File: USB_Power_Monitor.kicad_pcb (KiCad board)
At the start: 4 copper layers, 46.1 x 21 mm, 55 parts, among them IC1 MCS1826GQTE-05-P, J1 USB_C_Receptacle, J2 USB_C_Plug, J5 Conn_01x01, J6 Conn_01x01, U1 RP2040, U2 L7983PU33R, U3 W25Q16JVSS, U4 TS3USB221AQRSERQ1, Y1 ABM8-272-T3

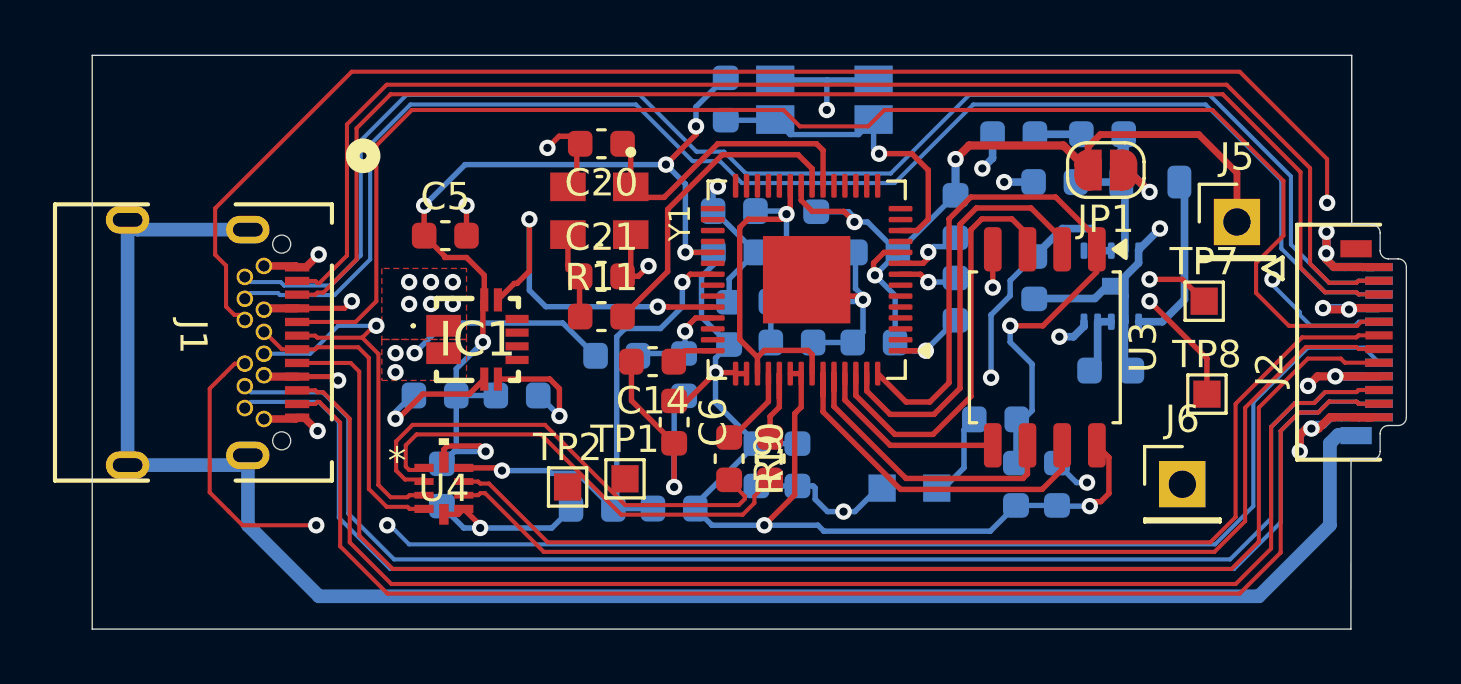
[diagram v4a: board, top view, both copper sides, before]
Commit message: Fixed overlapping silkscreen
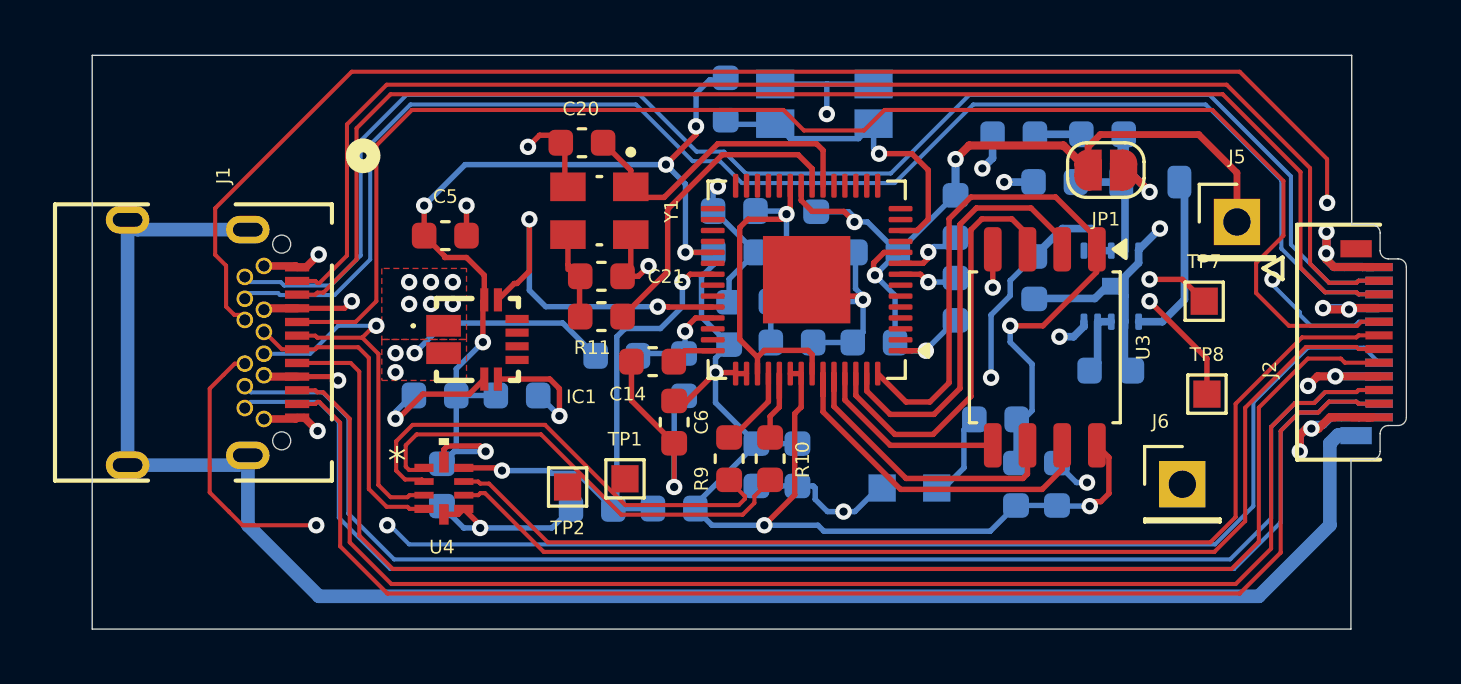
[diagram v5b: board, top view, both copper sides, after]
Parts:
- moved C20 0.71 mm to (144.9, 90.7)
- moved S1 0.15 mm to (153.8, 89.3)
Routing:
- net /XIN: track 10.8 -> 11.4 mm

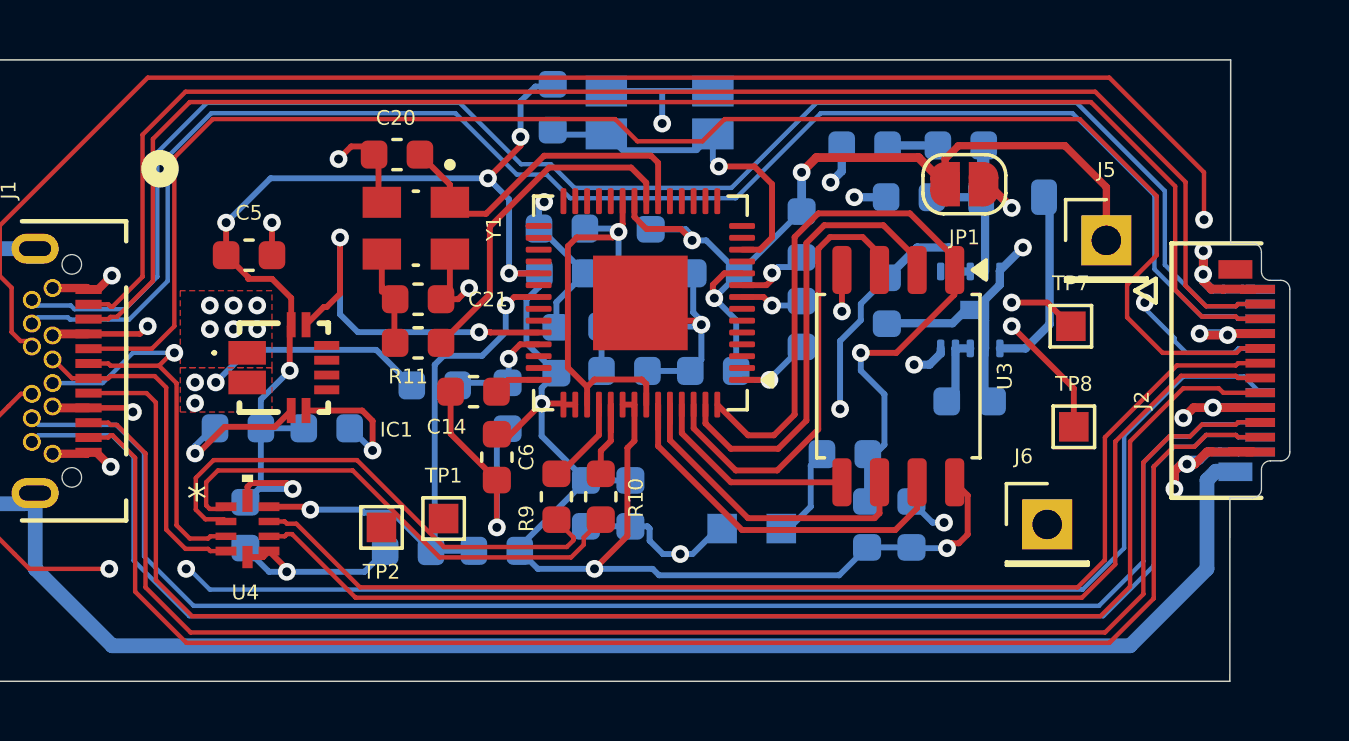
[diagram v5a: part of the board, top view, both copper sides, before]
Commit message: All DRC cleared except board outline and some weird footprint issues
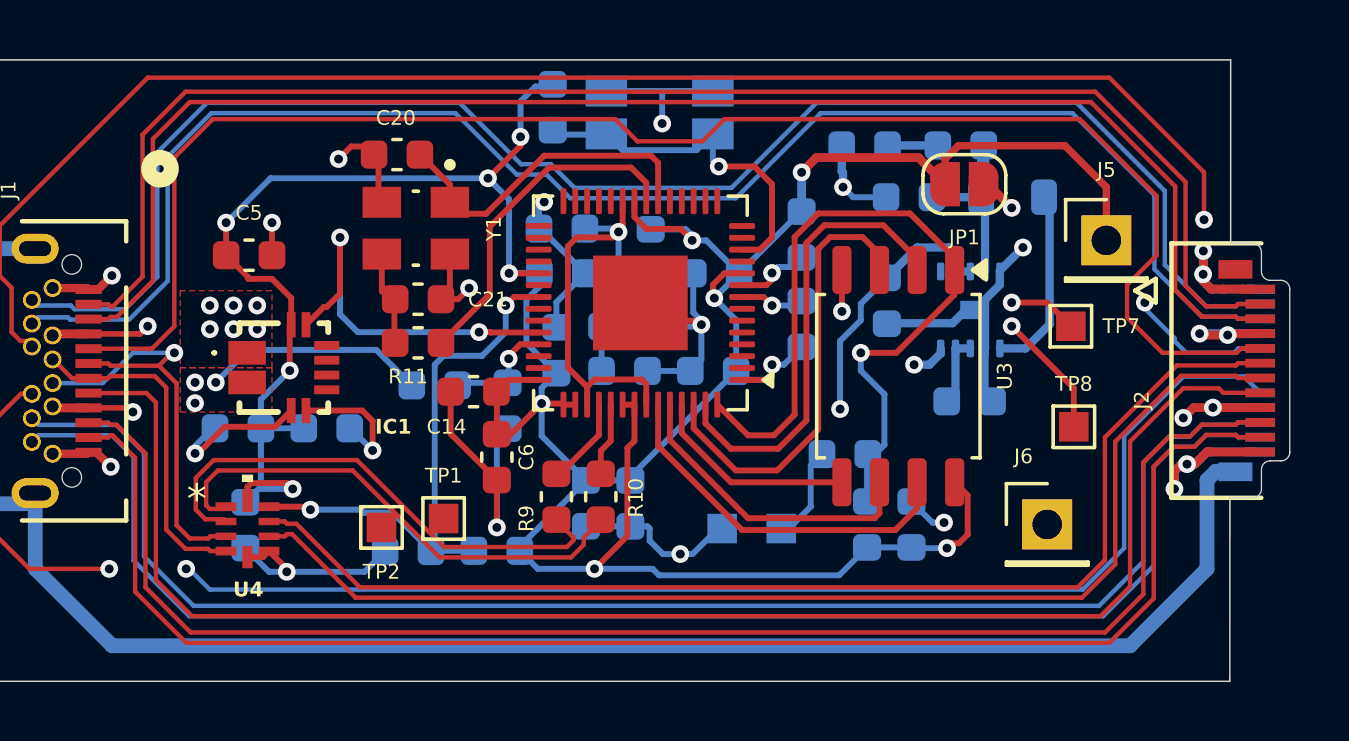
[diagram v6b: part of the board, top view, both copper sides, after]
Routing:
- net +3.3V: track 113.1 -> 120.5 mm
- net Net-(U1-USB_DP): track 3.38 -> 2.48 mm
- net /QSPI_SD3: track 13.3 -> 12.5 mm
- net /QSPI_SCLK: track 11.1 -> 10.5 mm
- net GND: track 87.0 -> 86.8 mm, vias 21 -> 20
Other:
- board text added: "*"
